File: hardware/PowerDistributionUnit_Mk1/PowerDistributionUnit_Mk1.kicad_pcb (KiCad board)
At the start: 4 copper layers, 80.4 x 206 mm, 767 parts, among them J1 XT-30, J10 Logic Analyzer, J11 Logic Analyzer, J12 Logic Analyzer, J13 Logic Analyzer, J2 Molex_NanoFit_2x8, J3 Molex_NanoFit_1x6, J4 Molex_NanoFit_1x2, J5 Molex_NanoFit_1x2, J6 Conn_01x01, J8 Molex_NanoFit_1x2, J9 Molex_NanoFit_1x2, Q1 NVMFWS1D7N04XMT1G, Q2 NVMFWS1D7N04XMT1G, SW1 JS202011SCQN, U1 LeaderSOM, U10 74LVC594APW,118, U11 TPS27SA08CQPWPRQ1, U12 TPS27SA08CQPWPRQ1, U13 TPS27SA08CQPWPRQ1, U14 TPS27SA08CQPWPRQ1, U15 TPS27SA08CQPWPRQ1, U16 TPS27SA08CQPWPRQ1, U17 TPS27SA08CQPWPRQ1, U18 TPS27SA08CQPWPRQ1, U19 TPS27SA08CQPWPRQ1, U2 LM74502HDDFR, U20 TPS27SA08CQPWPRQ1, U21 TPS27SA08CQPWPRQ1, U22 MCP23S17-E/SO, U23 ADS131M08QPBSRQ1, U24 ADS131M08QPBSRQ1, U25 NL17SZS11DFT2G-Q, U26 TLV9002QDRQ1, U27 74LVC594APW,118, U28 74LVC594APW,118, U29 74AUP1G04GW-Q100H, U3 TPS27SA08CQPWPRQ1, U30 NL27WZ17DFT2G-Q, U31 74LVC594APW,118, U32 ACS37042KLHBLT-010B3, U33 ACS37042KLHBLT-010B3, U34 ACS37042KLHBLT-010B3, U35 ACS37042KLHBLT-010B3, U36 ACS37042KLHBLT-010B3, U37 ACS37042KLHBLT-010B3, U38 ACS37042KLHBLT-010B3, U39 ACS37042KLHBLT-010B3, U4 TPS27SA08CQPWPRQ1, U40 ACS37042KLHBLT-010B3, U41 ACS37042KLHBLT-010B3, U42 ACS37042KLHBLT-010B3, U43 ACS37042KLHBLT-010B3, U44 ACS37042KLHBLT-010B3, U45 ACS37042KLHBLT-010B3, U46 ACS37042KLHBLT-010B3, U47 ACS37042KLHBLT-010B3, U5 TPS27SA08CQPWPRQ1, U6 TPS27SA08CQPWPRQ1, U7 74LVC594APW,118, U8 74LVC594APW,118, U9 TPS27SA08CQPWPRQ1, Y1 ABM3-8.000MHZ-D2Y-T, Y2 ABM3-8.000MHZ-D2Y-T

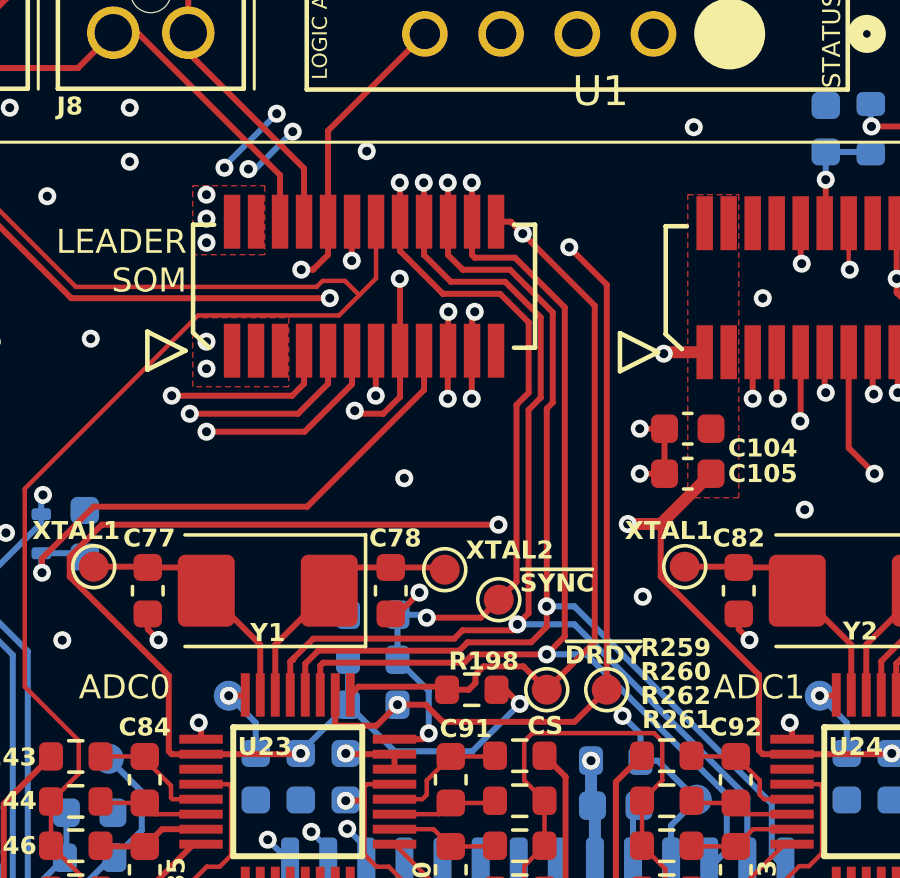
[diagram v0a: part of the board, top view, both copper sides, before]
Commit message: reroute LSOM SPI connections, repin logic analyzer connections
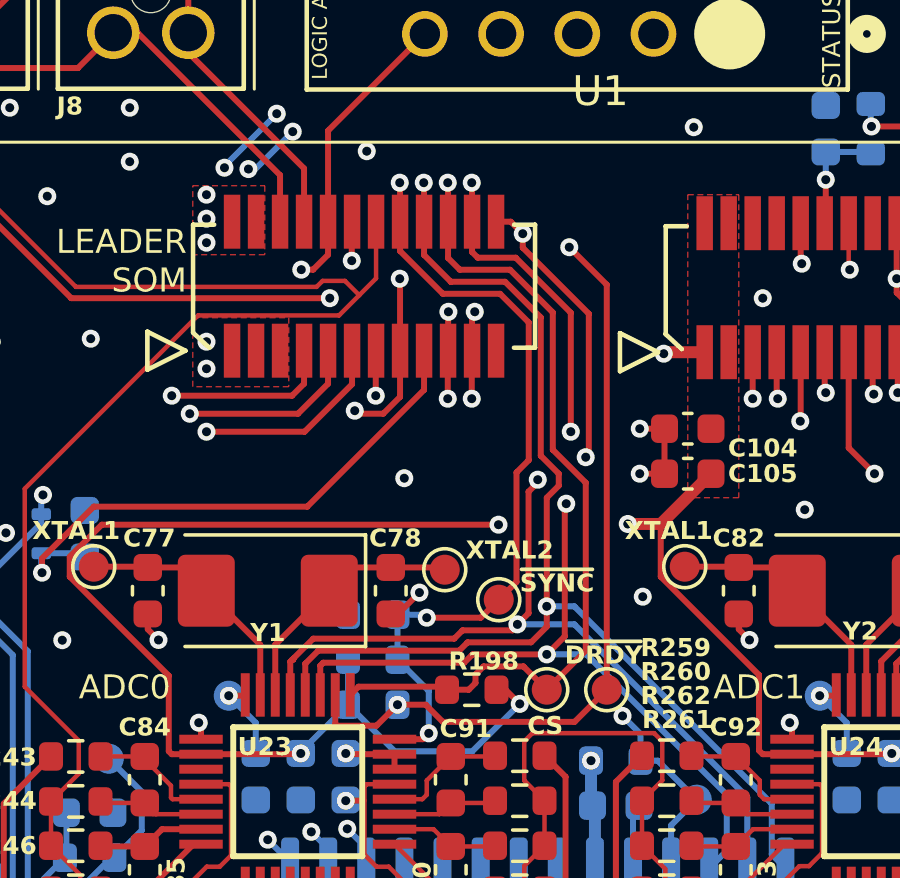
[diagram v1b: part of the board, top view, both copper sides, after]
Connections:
- J10 pad 6: /CS_SNS0 -> /CLK_2
- J10 pad 7: /MISO_2 -> /CS_SNS0
- J10 pad 8: /CLK_2 -> /MOSI_2
- J10 pad 9: /MOSI_2 -> /MISO_2
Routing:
- net /MOSI_2: track 62.1 -> 65.0 mm, vias 2 -> 4
- net /MISO_2: track 64.4 -> 62.8 mm
- net +3.3VA: track 73.0 -> 73.7 mm
- net /CLK_2: track 63.2 -> 63.3 mm, vias 2 -> 4
